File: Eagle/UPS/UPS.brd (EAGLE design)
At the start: 19.8 x 45.2 mm, 15 parts, among them K1 AQY21SOP, Q1 MOSFET-NCHANNEL2N7002PW, Q2 MOSFET-NCHANNEL2N7002PW, Q3 MOSFET-NCHANNEL2N7002PW

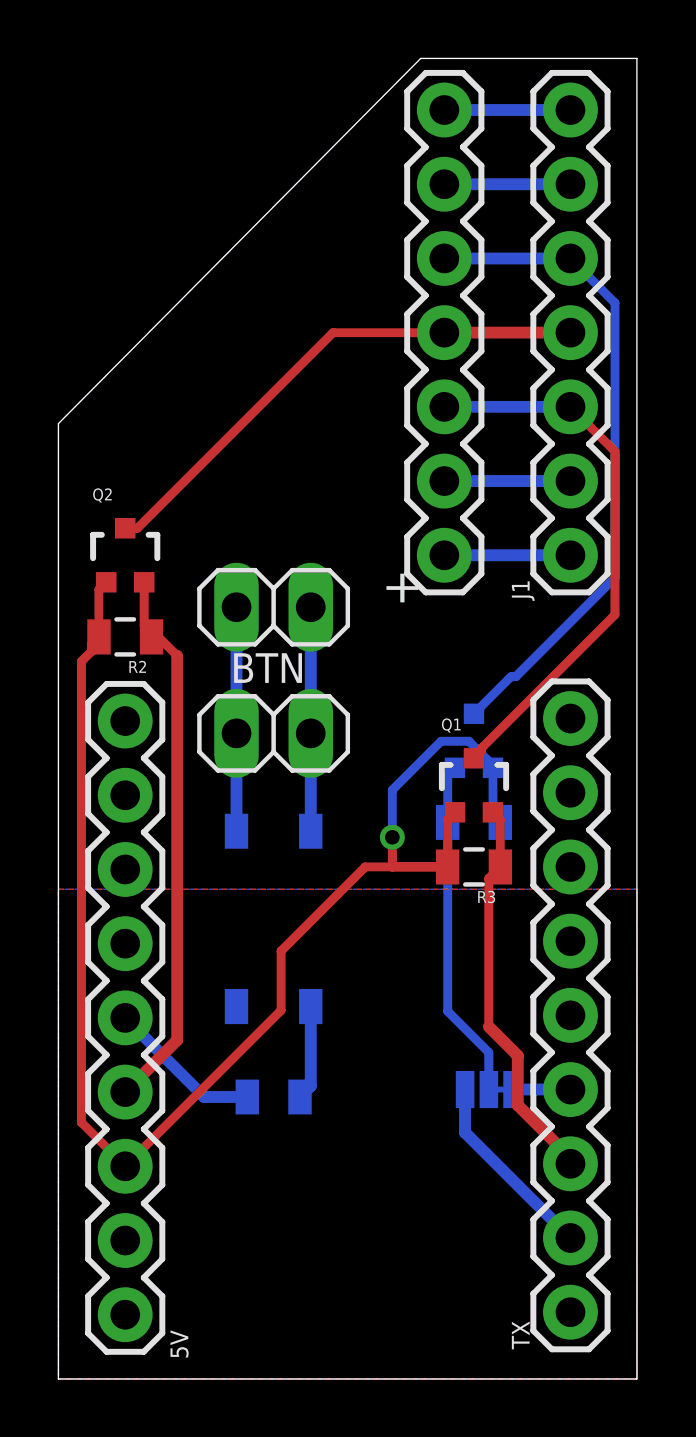
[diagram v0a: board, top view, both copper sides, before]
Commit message: Added another SSR for the DPST switch
Updated attributes and wire connections in UPS.brd.
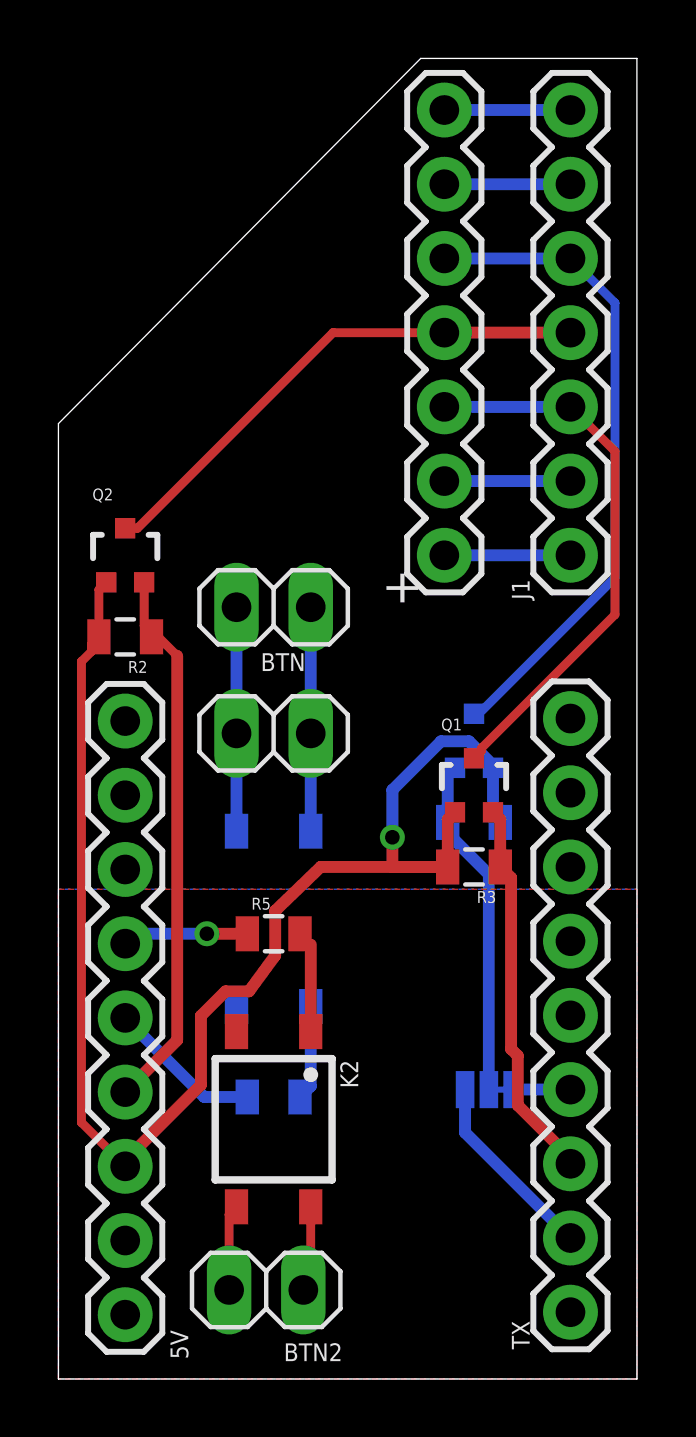
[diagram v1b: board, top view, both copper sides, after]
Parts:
- added BTN2: (no value), pinhead:1X02
- added K2: AQY21SOP, relay:SOP04
- added R5: (no value), SparkFun-Resistors:0805
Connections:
- removed net N$1: 5V.6
- new net BTN2: 5V.6, R5.1
- new net N$10: BTN2.2, K2.3
- new net N$11: K2.1, R5.2
- new net N$9: BTN2.1, K2.4
- net GND: now also K2.2
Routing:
- net BTN2: track 0.00 -> 4.32 mm, vias 0 -> 1
- net N$11: track 0.00 -> 3.50 mm
- net N$10: track 0.00 -> 2.95 mm
- net N$9: track 0.00 -> 2.95 mm
- net 3V3: track 50.5 -> 51.8 mm

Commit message: Rotated btn connector for more room
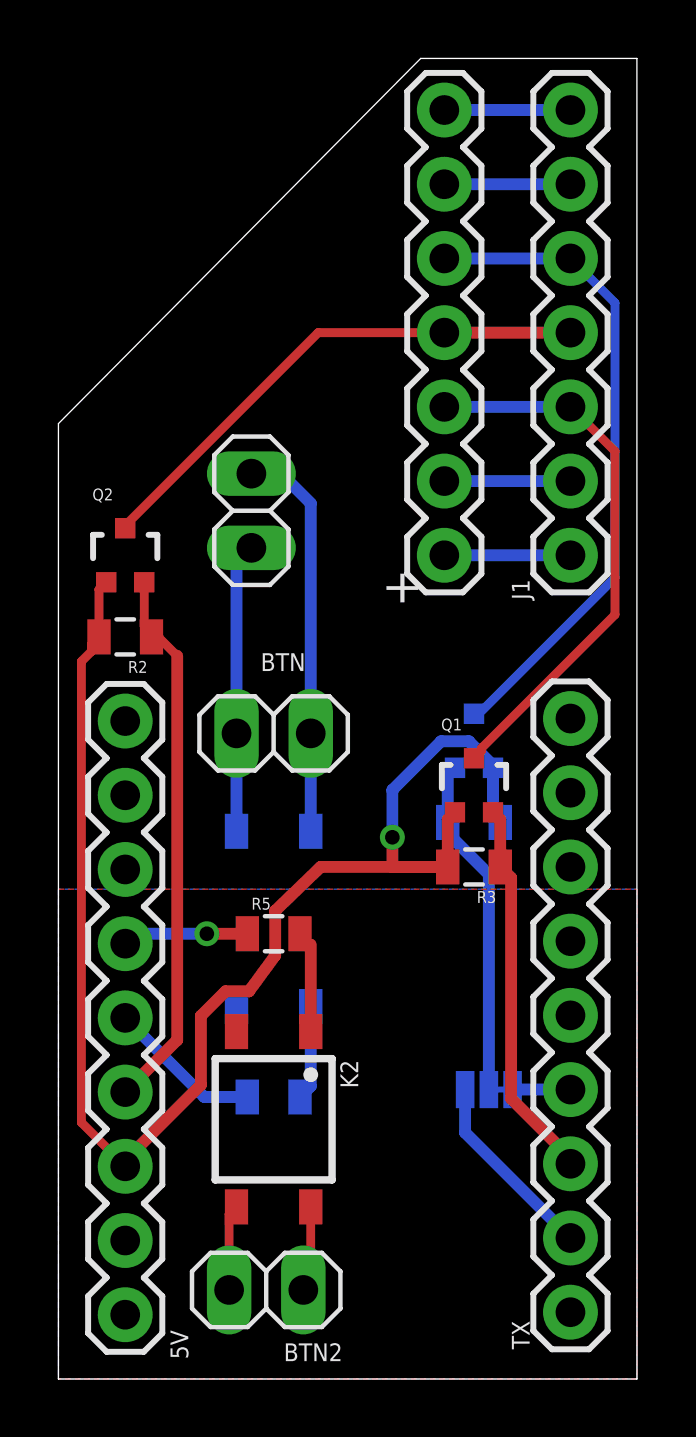
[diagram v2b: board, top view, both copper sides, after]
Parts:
- moved JP1 3.39 mm to (6.60, 29.7), turned to 270 degrees
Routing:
- net N$3: track 7.67 -> 13.7 mm
- net N$4: track 7.67 -> 9.91 mm
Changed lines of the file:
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@@
 <attribute name="VALUE" x="3.556" y="13.208" size="1.27" layer="28" rot="MR90"/>
 </element>
-<element name="JP1" library="pinhead" library_urn="urn:adsk.eagle:library:325" package="1X02" package3d_urn="urn:adsk.eagle:package:22435/2" value="" x="7.366" y="26.416" smashed="yes" rot="R180">
-<attribute name="POPULARITY" value="98" x="7.366" y="26.416" size="1.016" layer="27" ratio="14" rot="R180" display="off"/>
-<attribute name="VALUE" x="9.906" y="29.591" size="1.27" layer="27" rot="R180"/>
+<element name="JP1" library="pinhead" library_urn="urn:adsk.eagle:library:325" package="1X02" package3d_urn="urn:adsk.eagle:package:22435/2" value="" x="6.604" y="29.718" smashed="yes" rot="R270">
+<attribute name="POPULARITY" value="98" x="6.604" y="29.718" size="1.016" layer="27" ratio="14" rot="R270" display="off"/>
+<attribute name="VALUE" x="3.429" y="32.258" size="1.27" layer="27" rot="R270"/>
 </element>
 <element name="BTN" library="pinhead" library_urn="urn:adsk.eagle:library:325" package="1X02" package3d_urn="urn:adsk.eagle:package:22435/2" value="" x="7.366" y="22.098" smashed="yes" rot="R180">
@@
 <signal name="CS">
 <contactref element="TX" pad="3"/>
-<wire x1="15.7226" y1="11.0634" x2="15.494" y2="11.292" width="0.4064" layer="1"/>
 <wire x1="17.526" y1="7.566025" x2="17.526" y2="7.366" width="0.4064" layer="1"/>
-<wire x1="15.7226" y1="11.0634" x2="15.7226" y2="9.369425" width="0.4064" layer="1"/>
-<wire x1="15.7226" y1="9.369425" x2="17.526" y2="7.566025" width="0.4064" layer="1"/>
+<wire x1="15.494" y1="17.156" x2="15.494" y2="9.598025" width="0.4064" layer="1"/>
+<wire x1="15.494" y1="9.598025" x2="17.526" y2="7.566025" width="0.4064" layer="1"/>
 <contactref element="Q1" pad="2"/>
 <contactref element="R3" pad="1"/>
 <wire x1="15.124" y1="17.526" x2="15.494" y2="17.156" width="0.4064" layer="1"/>
-<wire x1="15.494" y1="17.156" x2="15.494" y2="11.292" width="0.4064" layer="1"/>
 <wire x1="15.124" y1="17.526" x2="15.124" y2="19.145" width="0.4064" layer="1"/>
 <wire x1="15.124" y1="19.145" x2="14.874" y2="19.395" width="0.4064" layer="1"/>
@@
 <contactref element="K1" pad="4"/>
 <wire x1="8.636" y1="18.748" x2="8.636" y2="22.098" width="0.4064" layer="16"/>
-<wire x1="8.636" y1="26.416" x2="8.636" y2="22.098" width="0.4064" layer="16"/>
+<wire x1="8.636" y1="22.098" x2="8.636" y2="29.972" width="0.4064" layer="16"/>
+<wire x1="8.636" y1="29.972" x2="7.62" y2="30.988" width="0.4064" layer="16"/>
+<wire x1="7.62" y1="30.988" x2="6.604" y2="30.988" width="0.4064" layer="16"/>
 </signal>
 <signal name="N$4">
@@
 <contactref element="BTN" pad="2"/>
 <wire x1="6.096" y1="18.748" x2="6.096" y2="22.098" width="0.4064" layer="16"/>
-<wire x1="6.096" y1="26.416" x2="6.096" y2="22.098" width="0.4064" layer="16"/>
+<wire x1="6.604" y1="28.448" x2="6.096" y2="27.94" width="0.4064" layer="16"/>
+<wire x1="6.096" y1="22.098" x2="6.096" y2="27.94" width="0.4064" layer="16"/>
 </signal>
 <signal name="BTN">
@@
 <contactref element="J1" pad="4"/>
 <contactref element="+" pad="4"/>
-<wire x1="9.398" y1="35.814" x2="17.526" y2="35.814" width="0.3048" layer="1"/>
-<wire x1="9.398" y1="35.814" x2="2.703" y2="29.119" width="0.3048" layer="1"/>
-<wire x1="2.286" y1="29.119" x2="2.703" y2="29.119" width="0.3048" layer="1"/>
+<wire x1="8.89" y1="35.814" x2="17.526" y2="35.814" width="0.3048" layer="1"/>
+<wire x1="8.89" y1="35.814" x2="2.286" y2="29.21" width="0.3048" layer="1"/>
+<wire x1="2.286" y1="29.119" x2="2.286" y2="29.21" width="0.3048" layer="1"/>
 <wire x1="17.526" y1="35.814" x2="13.208" y2="35.814" width="0.4064" layer="1"/>
 <contactref element="Q2" pad="3"/>
